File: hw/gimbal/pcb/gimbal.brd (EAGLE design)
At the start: 60 x 42 mm, 80 parts, among them J1 JST-XH4SMT_RA, T12 TPPAD1-13, T3 TPPAD1-13, T8 TPPAD1-13, U1 STM32F4R_64PIN, U2 TPS62172PWSON8, U3 TPS55330PQFN16, U4 MC33926, U5 DRV8313, U6 DRV8313, U7 AS5048A

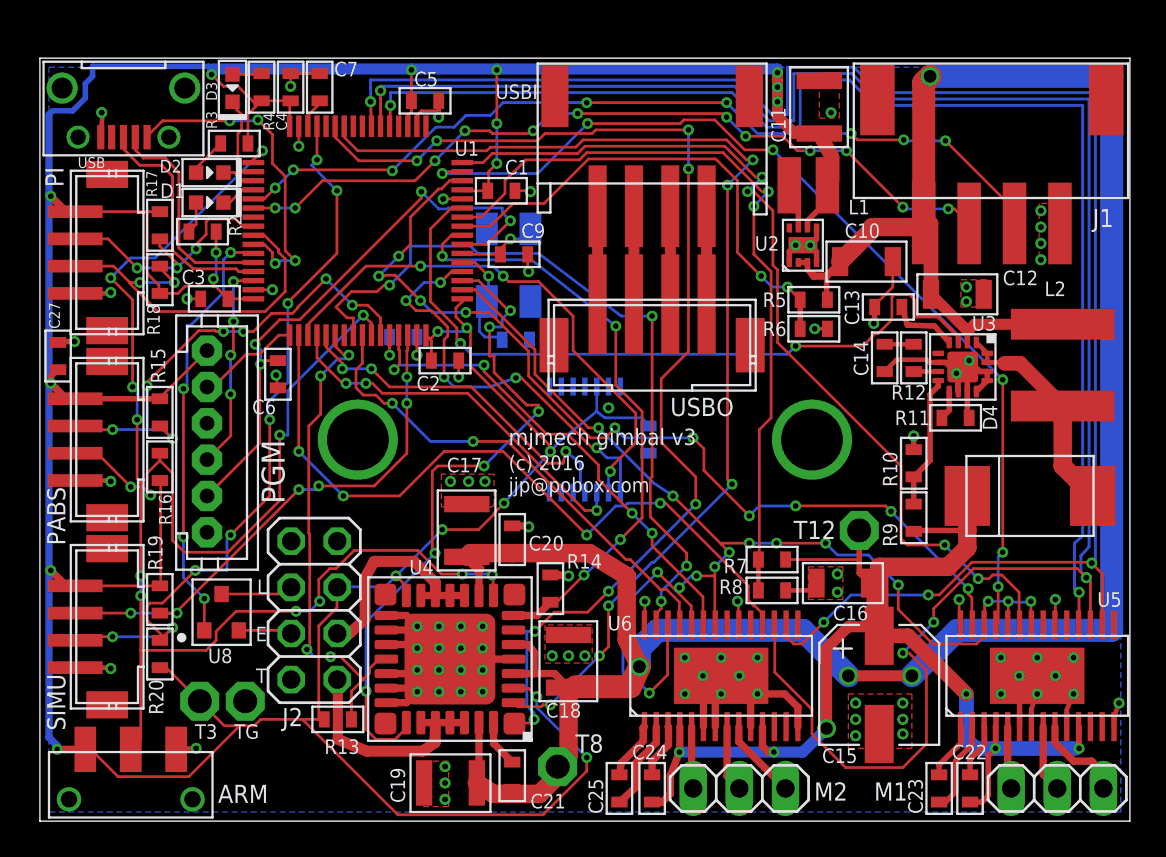
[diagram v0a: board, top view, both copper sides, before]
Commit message: gimbal: Start work on updating gimbal board to support mounting a joule shield on top of it.
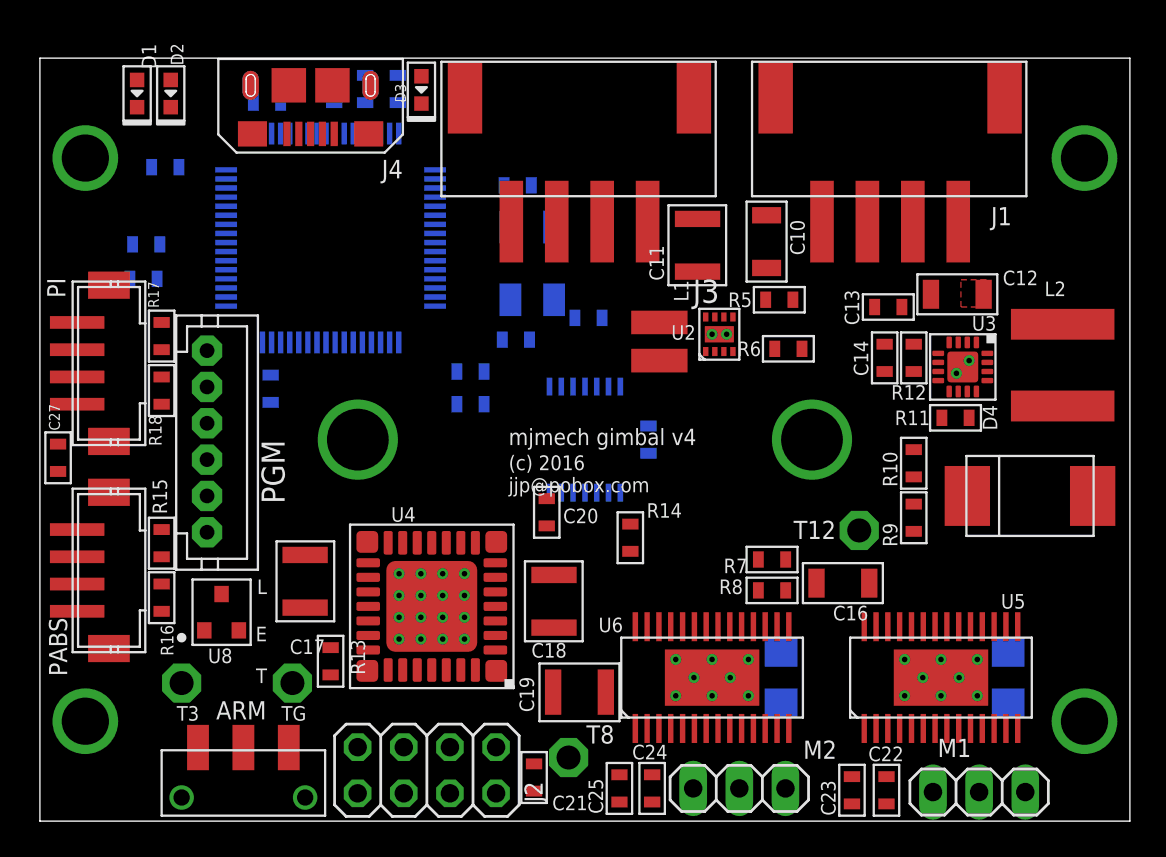
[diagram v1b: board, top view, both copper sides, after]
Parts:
- removed C15: 100uF, mfpassives:CP6.3MM
- removed R19, R20: 1.69k, mfpassives:R0603
- removed SIMU: JST-ZH4, gimbal:JST_ZH_SMT_VERT_4
- removed USB: MICRO-USB, gimbal:FCI_MICROUSB_SMT_RA
- removed USBI: (no value), gimbal:JST_PH_SMT_RA_4
- removed USBO: (no value), gimbal:JST_PH_SMT_VERT_4
- added C28, C29: 47uF, rcl:C1206
- added J3: JST-XH4SMT_RA, gimbal:JST_XH_SMT_RA_4
- added J4: MF-CON-MICROUSB-RIGHT, mf_connectors:MICROUSB-RIGHT
- added U$52, U$53, U$54, U$55: M2.5MOUNT, joule_shield:M2.5MOUNT
- moved L1 11.9 mm to (34.1, 26.4), turned to 90 degrees
- moved J2 10.8 mm to (21.3, 2.80), turned to 180 degrees
- moved D3 10.4 mm to (21.0, 40.2)
- moved C11 10.1 mm to (36.2, 31.7)
- moved C17 9.33 mm to (14.6, 13.2), turned to 270 degrees
- moved C5 8.70 mm to (12.5, 39.5), flipped to the bottom, turned to 180 degrees
- moved C19 8.68 mm to (29.7, 7.10)
- moved R4 7.50 mm to (19.7, 40.3), flipped to the bottom
- moved D1 7.21 mm to (5.35, 40.0), turned to 90 degrees
- moved PABS 7.20 mm to (2.80, 13.8)
- moved R15 7.20 mm to (6.70, 15.3)
- moved R16 7.20 mm to (6.70, 12.3)
- moved U2 6.72 mm to (37.4, 26.8)
- moved ARM 6.20 mm to (11.2, 1.30)
- moved PI 6.10 mm to (2.80, 25.2)
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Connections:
- removed net N$12: USBI.1, USBO.1
- removed net N$13: USBI.2, USBO.2
- removed net N$14: USBI.3, USBO.3
- removed net N$15: USBI.4, USBO.4
- net +12V: now also C28.1, C29.1; no longer C15.P$1
- net +3V3: no longer R19.P$2, R20.P$2, SIMU.1
- net +8V: now also J3.4
- net GND: now also C28.2, C29.2, J3.1, J4.5, J4.S1, J4.S2, J4.S3, J4.S4, J4.S5, J4.S6; no longer C15.P$2, SIMU.4, USB.5
- net SIMU_SCL: no longer R20.P$1, SIMU.3
- net SIMU_SDA: no longer R19.P$1, SIMU.2
- net SLAVE_RX: now also J3.3
- net SLAVE_TX: now also J3.2
- net USB_DM: now also J4.2; no longer USB.2
- net USB_DP: now also J4.3; no longer USB.3
- net USB_VBUS: now also J4.1; no longer USB.1
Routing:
- net +3V3: track 247.9 -> 0.00 mm, vias 22 -> 0
- net +8V: track 145.6 -> 0.00 mm, vias 4 -> 0
- net BLDC_SLEEP/: track 107.4 -> 0.00 mm, vias 4 -> 0
- net BLDC_RESET/: track 95.6 -> 0.00 mm, vias 4 -> 0
- net GND: track 90.8 -> 0.00 mm, vias 52 -> 0
- net BLDC_FAULT1: track 72.9 -> 0.00 mm, vias 2 -> 0
- net BLDC_EN: track 69.4 -> 0.00 mm, vias 15 -> 0
- net +12V: track 69.3 -> 0.00 mm, vias 6 -> 0
- net MOTOR_EN: track 63.4 -> 0.00 mm, vias 10 -> 0
- net AGITATOR_PWM: track 61.7 -> 0.00 mm, vias 8 -> 0
- net AEG_PWM: track 61.2 -> 0.00 mm, vias 6 -> 0
- net MOTOR1_IN2: track 52.8 -> 0.00 mm, vias 6 -> 0
- net MOTOR1_IN1: track 51.8 -> 0.00 mm, vias 10 -> 0
- net MOTOR1_IN3: track 51.2 -> 0.00 mm, vias 4 -> 0
- net SLAVE_TX: track 47.3 -> 0.00 mm, vias 8 -> 0
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- removed copper zone on layer 16, net GND
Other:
- board text added: "mjmech gimbal v4"
- board text removed: "mjmech gimbal v3"

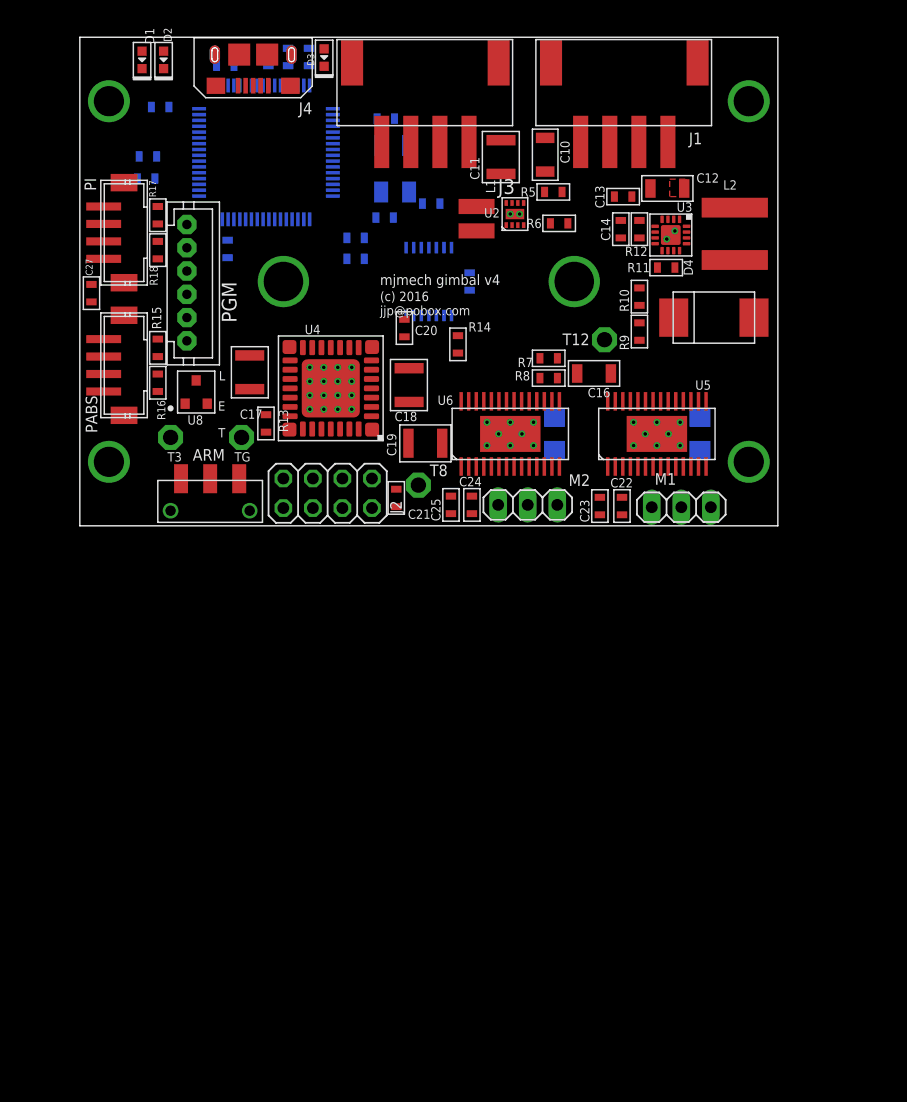
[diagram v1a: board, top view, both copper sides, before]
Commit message: gimbal: Move parts around to roughly correct location and add in plane polygons.
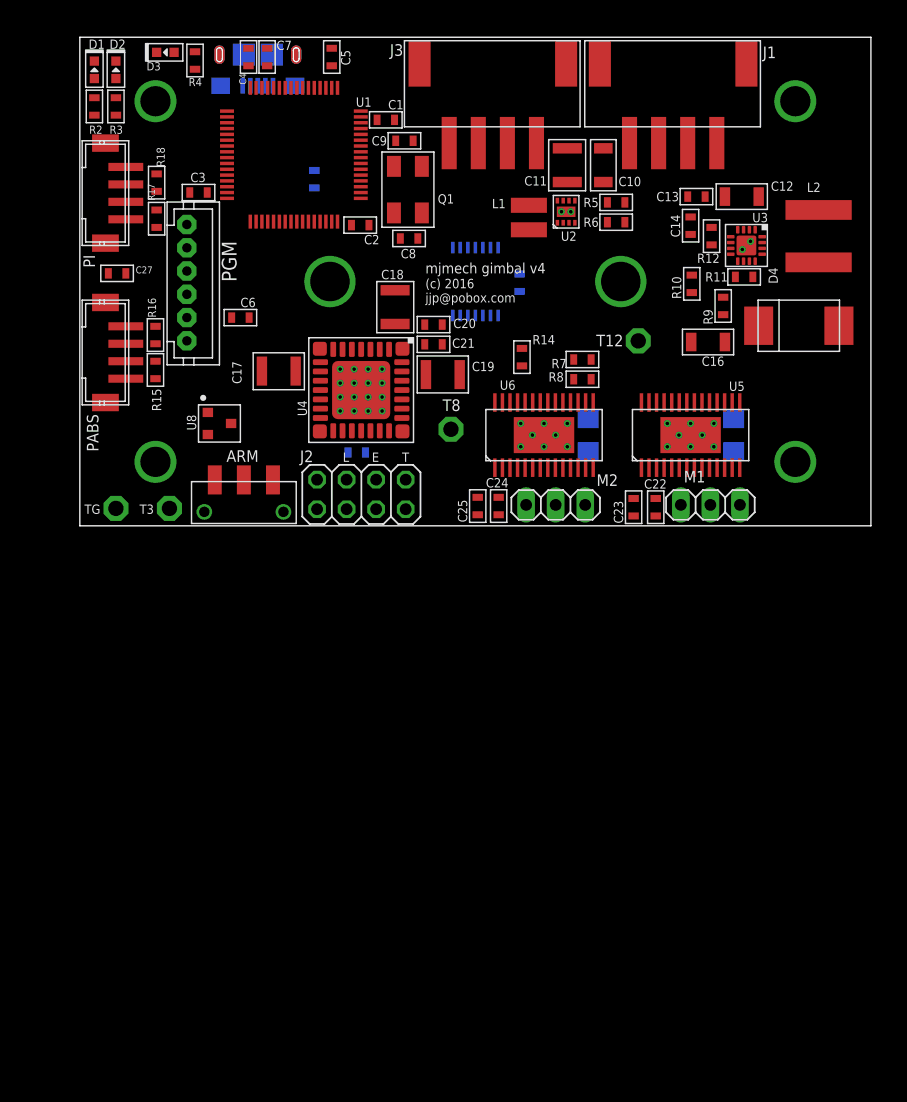
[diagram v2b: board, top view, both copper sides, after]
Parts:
- moved D3 13.7 mm to (7.35, 40.7), turned to 0 degrees
- moved C21 13.6 mm to (30.4, 15.6), turned to 180 degrees
- moved TG 12.4 mm to (3.10, 1.50)
- moved C16 10.2 mm to (54.0, 15.8)
- moved R4 9.80 mm to (9.90, 40.0), flipped to the top
- moved C5 9.18 mm to (21.6, 40.3), flipped to the top, turned to 270 degrees
- moved R13 8.19 mm to (23.8, 6.30), flipped to the bottom, turned to 0 degrees
- moved R1 7.72 mm to (20.1, 29.8), turned to 270 degrees
- moved R9 7.53 mm to (55.3, 18.9)
- moved D4 7.33 mm to (61.8, 17.2)
- moved L2 7.20 mm to (63.5, 24.9)
- moved C18 6.81 mm to (27.1, 18.8), turned to 270 degrees
- moved R11 6.75 mm to (57.1, 21.4)
- moved U3 6.56 mm to (57.3, 24.1)
- moved C12 6.44 mm to (56.9, 28.3)
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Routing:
- added copper zone on layer 15, net +3V3
- added copper zone on layer 2, net GND
- removed copper zone on layer 1, net GND
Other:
- board size 60 x 42 mm -> 68 x 42 mm

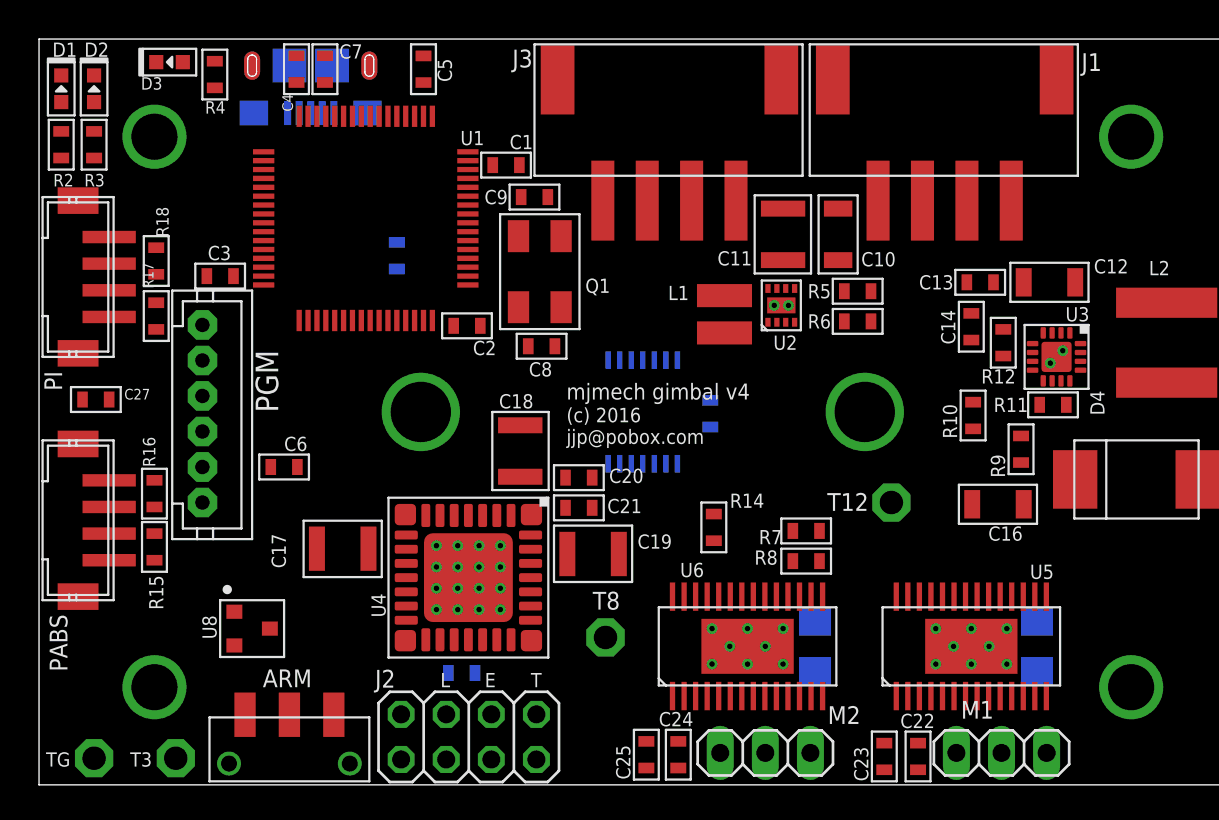
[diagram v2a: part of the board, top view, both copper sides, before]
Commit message: gimbal: More work on v4 layout.
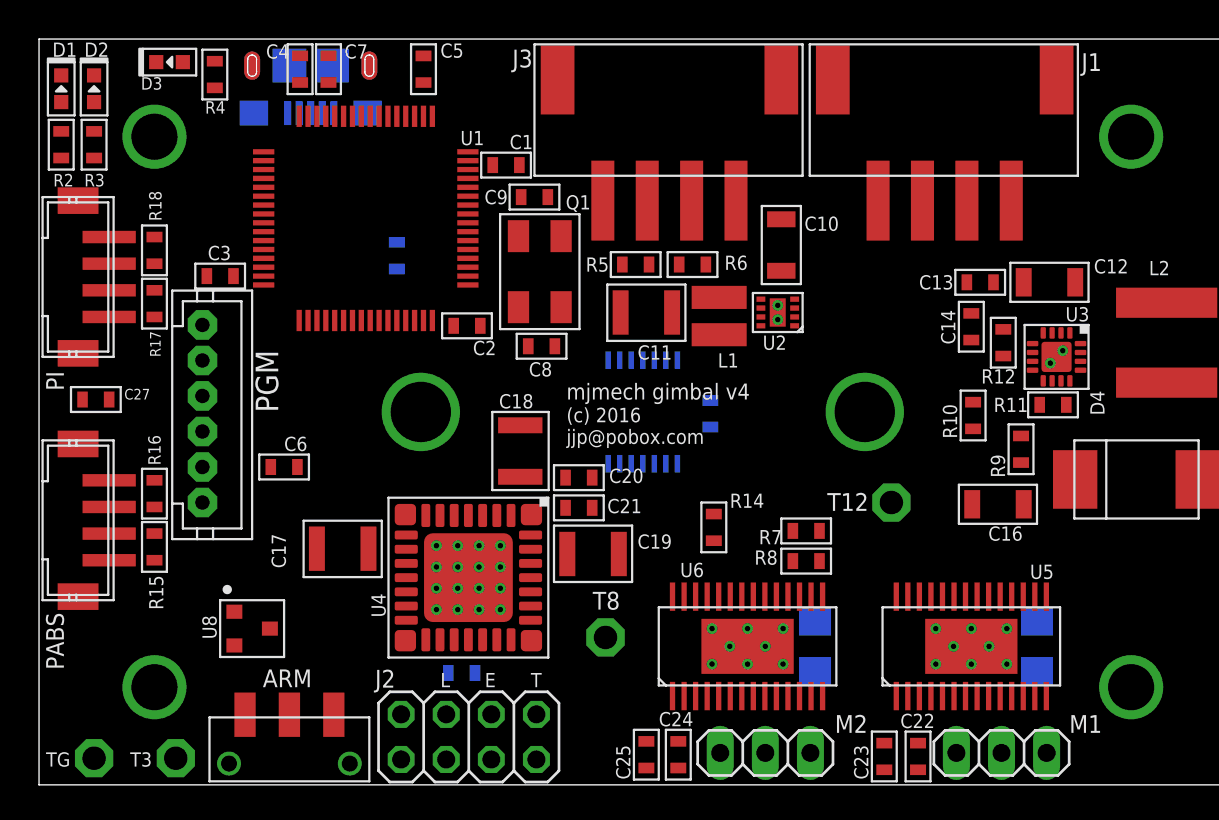
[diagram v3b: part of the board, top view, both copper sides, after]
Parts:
- moved R5 12.6 mm to (33.6, 29.3), turned to 180 degrees
- moved R6 9.84 mm to (36.8, 29.3)
- moved C11 8.87 mm to (34.2, 26.6), turned to 180 degrees
- moved C10 3.26 mm to (41.8, 30.4)
- moved R17 0.71 mm to (6.50, 27.1), turned to 270 degrees
- moved R18 0.61 mm to (6.50, 30.1)
- moved U2 0.45 mm to (41.6, 26.6), turned to 180 degrees
- moved L1 0.32 mm to (38.3, 26.4)
- moved C4 0.20 mm to (14.7, 40.3)
- moved C7 0.20 mm to (16.3, 40.3)

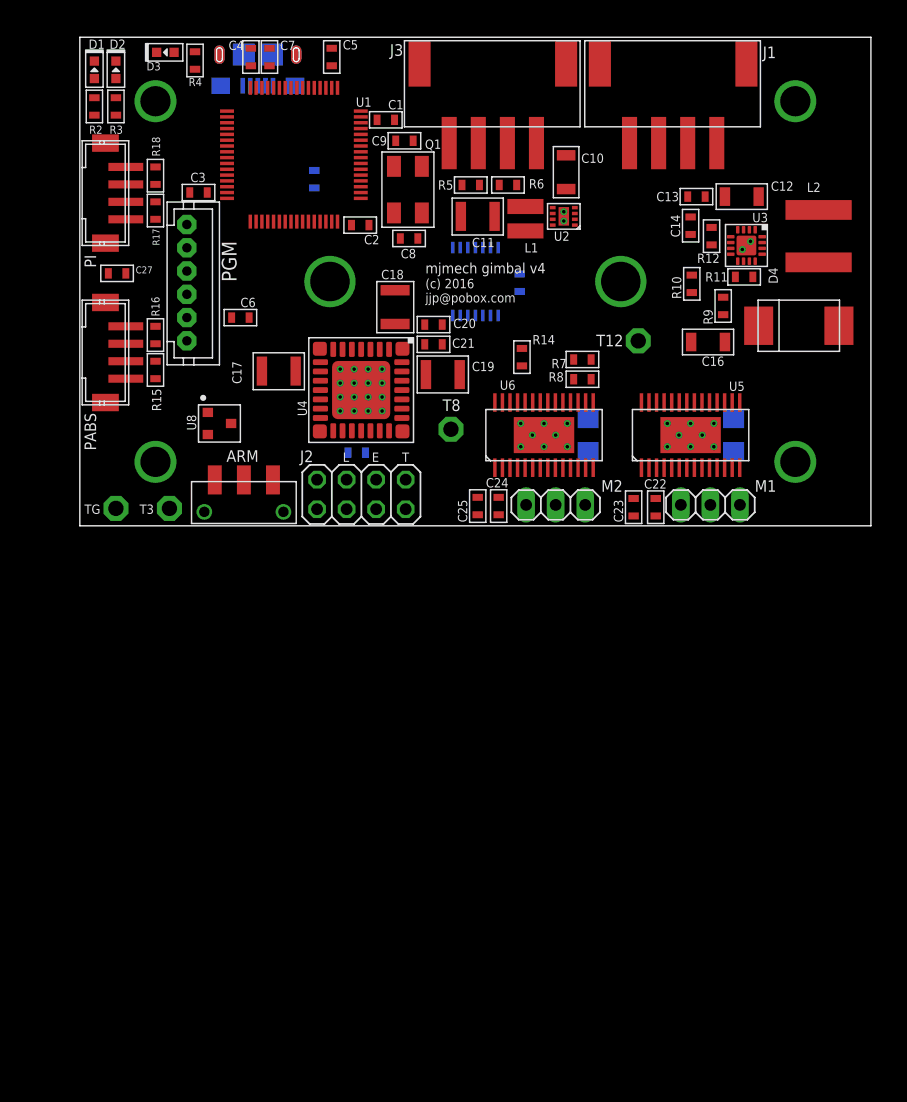
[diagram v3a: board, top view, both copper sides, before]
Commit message: gimbal: Route most power and grounds.
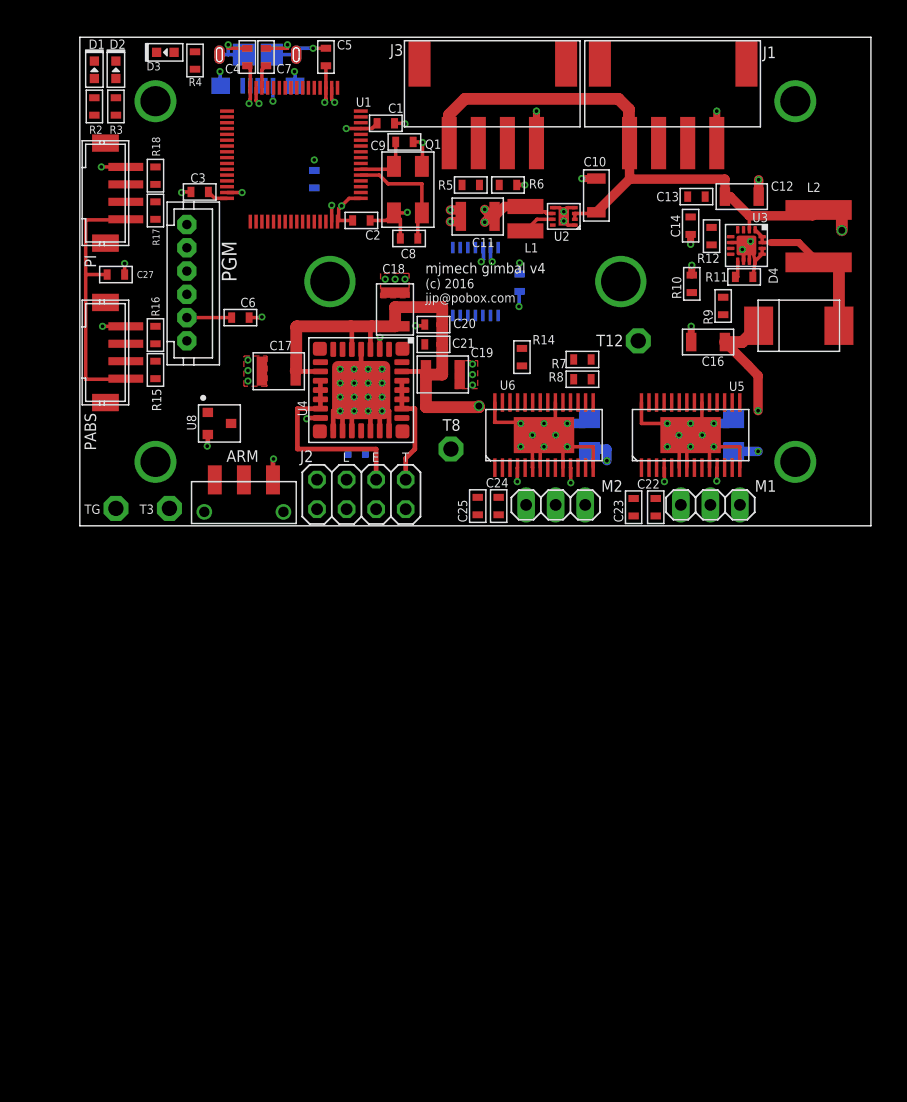
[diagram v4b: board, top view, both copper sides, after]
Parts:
- moved C10 3.28 mm to (44.4, 28.4), turned to 90 degrees
- moved T8 1.70 mm to (31.9, 6.60)
- moved C5 0.50 mm to (21.1, 40.3), turned to 90 degrees
- moved C2 0.41 mm to (24.2, 26.2)
- moved C7 0.30 mm to (16.0, 40.3)
- moved C4 0.30 mm to (14.4, 40.3)
- moved C1 0.30 mm to (26.3, 34.6)
- moved C18 0.20 mm to (27.1, 18.6), turned to 90 degrees
- moved C27 0.14 mm to (3.10, 21.6), turned to 0 degrees
- moved C3 0.11 mm to (10.3, 28.7), turned to 180 degrees
- moved C9 0.10 mm to (27.9, 33.0)
- moved C28 0.10 mm to (43.8, 7.80)
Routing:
- net +8V: track 0.00 -> 142.3 mm, vias 0 -> 2
- net GND: track 0.00 -> 130.4 mm, vias 0 -> 43
- net +12V: track 0.00 -> 52.4 mm, vias 0 -> 7
- net +3V3: track 0.00 -> 50.5 mm, vias 0 -> 10
- net N$2: track 0.00 -> 17.2 mm
- net N$17: track 0.00 -> 14.1 mm
- net N$35: track 0.00 -> 10.4 mm
- net N$3: track 0.00 -> 9.95 mm
- net N$36: track 0.00 -> 5.12 mm
- net N$24: track 0.00 -> 3.85 mm
- net N$16: track 0.00 -> 2.76 mm
- net N$23: track 0.00 -> 2.04 mm
- net N$18: track 0.00 -> 1.55 mm
- added copper zone on layer 1, net GND
